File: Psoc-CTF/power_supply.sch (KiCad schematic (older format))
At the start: 17 parts, among them J1 Conn_01x02, J2 Conn_01x03, U1 AMS1117-5.0, U2 AMS1117-3.3, U6 AMS1117-3.3

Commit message: Corrrecciones y anexo de logo
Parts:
- added R46, R47: 0, Resistor_SMD:R_0805_2012Metric_Pad1.20x1.40mm_HandSolder, symbol Device:R
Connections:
- net +3V3: now also R47.2; no longer C40.1, U6.2 (VO)
- net +5V: now also R46.2; no longer U6.3 (VI)
- new net: C40.1, R47.1, U6.2 (VO)
- new net: R46.1, U6.3 (VI)
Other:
- moved on the sheet: C40, C41, U6
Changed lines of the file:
@@
 L power:+3V3 #PWR014
 U 1 1 62395ED8
-P 5075 4575
-F 0 "#PWR014" H 5075 4425 50  0001 C CNN
-F 1 "+3V3" H 5090 4748 50  0000 C CNN
-F 2 "" H 5075 4575 50  0001 C CNN
-F 3 "" H 5075 4575 50  0001 C CNN
-	1    5075 4575
+P 5250 4175
+F 0 "#PWR014" H 5250 4025 50  0001 C CNN
+F 1 "+3V3" H 5265 4348 50  0000 C CNN
+F 2 "" H 5250 4175 50  0001 C CNN
+F 3 "" H 5250 4175 50  0001 C CNN
+	1    5250 4175
 	1    0    0    -1
 $EndComp
-Connection ~ 4250 4875
+Connection ~ 4425 4475
 $Comp
 L power:GND #PWR013
 U 1 1 6239862F
-P 4250 4875
-F 0 "#PWR013" H 4250 4625 50  0001 C CNN
-F 1 "GND" H 4255 4702 50  0000 C CNN
-F 2 "" H 4250 4875 50  0001 C CNN
-F 3 "" H 4250 4875 50  0001 C CNN
-	1    4250 4875
+P 4425 4475
+F 0 "#PWR013" H 4425 4225 50  0001 C CNN
+F 1 "GND" H 4430 4302 50  0000 C CNN
+F 2 "" H 4425 4475 50  0001 C CNN
+F 3 "" H 4425 4475 50  0001 C CNN
+	1    4425 4475
 	1    0    0    -1
 $EndComp
-Connection ~ 4625 4875
+Connection ~ 4800 4475
 Wire Wire Line
-	4625 4875 5075 4875
+	4800 4475 5250 4475
 Wire Wire Line
-	4250 4875 4625 4875
-Connection ~ 4625 4575
+	4425 4475 4800 4475
 Wire Wire Line
-	4625 4575 5075 4575
-Wire Wire Line
-	4550 4575 4625 4575
+	4725 4175 4800 4175
 $Comp
 L Device:C C41
 U 1 1 6239863B
-P 5075 4725
-F 0 "C41" H 5190 4771 50  0000 L CNN
-F 1 "10uF" H 5190 4680 50  0000 L CNN
-F 2 "Capacitor_SMD:C_0603_1608Metric_Pad1.08x0.95mm_HandSolder" H 5113 4575 50  0001 C CNN
-F 3 "~" H 5075 4725 50  0001 C CNN
-	1    5075 4725
+P 5250 4325
+F 0 "C41" H 5365 4371 50  0000 L CNN
+F 1 "10uF" H 5365 4280 50  0000 L CNN
+F 2 "Capacitor_SMD:C_0603_1608Metric_Pad1.08x0.95mm_HandSolder" H 5288 4175 50  0001 C CNN
+F 3 "~" H 5250 4325 50  0001 C CNN
+	1    5250 4325
 	1    0    0    -1
 $EndComp
@@
 L Device:CP C40
 U 1 1 62398641
-P 4625 4725
-F 0 "C40" H 4743 4771 50  0000 L CNN
-F 1 "10uF" H 4743 4680 50  0000 L CNN
-F 2 "Capacitor_SMD:C_0805_2012Metric_Pad1.18x1.45mm_HandSolder" H 4663 4575 50  0001 C CNN
-F 3 "~" H 4625 4725 50  0001 C CNN
-	1    4625 4725
+P 4800 4325
+F 0 "C40" H 4918 4371 50  0000 L CNN
+F 1 "10uF" H 4918 4280 50  0000 L CNN
+F 2 "Capacitor_SMD:C_0805_2012Metric_Pad1.18x1.45mm_HandSolder" H 4838 4175 50  0001 C CNN
+F 3 "~" H 4800 4325 50  0001 C CNN
+	1    4800 4325
 	1    0    0    -1
 $EndComp
-Wire Wire Line
-	3800 4575 3950 4575
 $Comp
 L Regulator_Linear:AMS1117-3.3 U6
 U 1 1 62398648
-P 4250 4575
-F 0 "U6" H 4250 4817 50  0000 C CNN
-F 1 "AMS1117-3.3" H 4250 4726 50  0000 C CNN
-F 2 "Package_TO_SOT_SMD:SOT-223-3_TabPin2" H 4250 4775 50  0001 C CNN
-F 3 "http://www.advanced-monolithic.com/pdf/ds1117.pdf" H 4350 4325 50  0001 C CNN
-	1    4250 4575
+P 4425 4175
+F 0 "U6" H 4425 4417 50  0000 C CNN
+F 1 "AMS1117-3.3" H 4425 4326 50  0000 C CNN
+F 2 "Package_TO_SOT_SMD:SOT-223-3_TabPin2" H 4425 4375 50  0001 C CNN
+F 3 "http://www.advanced-monolithic.com/pdf/ds1117.pdf" H 4525 3925 50  0001 C CNN
+	1    4425 4175
 	1    0    0    -1
 $EndComp
-Text Notes 3900 4200 0    62   ~ 0
+Text Notes 4075 3800 0    62   ~ 0
 ESP POWER SUPPLY
 $Comp
 L power:+5V #PWR012
 U 1 1 62398656
-P 3800 4575
-F 0 "#PWR012" H 3800 4425 50  0001 C CNN
-F 1 "+5V" H 3800 4750 50  0000 C CNN
-F 2 "" H 3800 4575 50  0001 C CNN
-F 3 "" H 3800 4575 50  0001 C CNN
-	1    3800 4575
+P 3575 4150
+F 0 "#PWR012" H 3575 4000 50  0001 C CNN
+F 1 "+5V" H 3575 4325 50  0000 C CNN
+F 2 "" H 3575 4150 50  0001 C CNN
+F 3 "" H 3575 4150 50  0001 C CNN
+	1    3575 4150
 	1    0    0    -1
 $EndComp
-Connection ~ 5075 4575
+$Comp
+L Device:R R?
+U 1 1 624179B2
+P 3775 4175
+AR Path="/624179B2" Ref="R?"  Part="1"
+AR Path="/620E3406/624179B2" Ref="R46"  Part="1"
+F 0 "R46" V 3875 4175 50  0000 C CNN
+F 1 "0" V 3950 4175 50  0000 C CNN
+F 2 "Resistor_SMD:R_0805_2012Metric_Pad1.20x1.40mm_HandSolder" V 3705 4175 50  0001 C CNN
+F 3 "~" H 3775 4175 50  0001 C CNN
+	1    3775 4175
+	0    1    1    0
+$EndComp
+Wire Wire Line
+	3575 4150 3575 4175
+Wire Wire Line
+	3575 4175 3625 4175
+Wire Wire Line
+	3925 4175 4125 4175
+$Comp
+L Device:R R?
+U 1 1 62419A9D
+P 5025 4175
+AR Path="/62419A9D" Ref="R?"  Part="1"
+AR Path="/620E3406/62419A9D" Ref="R47"  Part="1"
+F 0 "R47" V 5125 4175 50  0000 C CNN
+F 1 "0" V 5200 4175 50  0000 C CNN
+F 2 "Resistor_SMD:R_0805_2012Metric_Pad1.20x1.40mm_HandSolder" V 4955 4175 50  0001 C CNN
+F 3 "~" H 5025 4175 50  0001 C CNN
+	1    5025 4175
+	0    -1   -1   0
+$EndComp
+Wire Wire Line
+	4875 4175 4800 4175
+Connection ~ 4800 4175
+Wire Wire Line
+	5175 4175 5250 4175
+Connection ~ 5250 4175
+Wire Notes Line
+	3450 3600 3450 4700
+Wire Notes Line
+	3450 4700 5600 4700
+Wire Notes Line
+	5600 4700 5600 3600
+Wire Notes Line
+	5600 3600 3450 3600
 $EndSCHEMATC

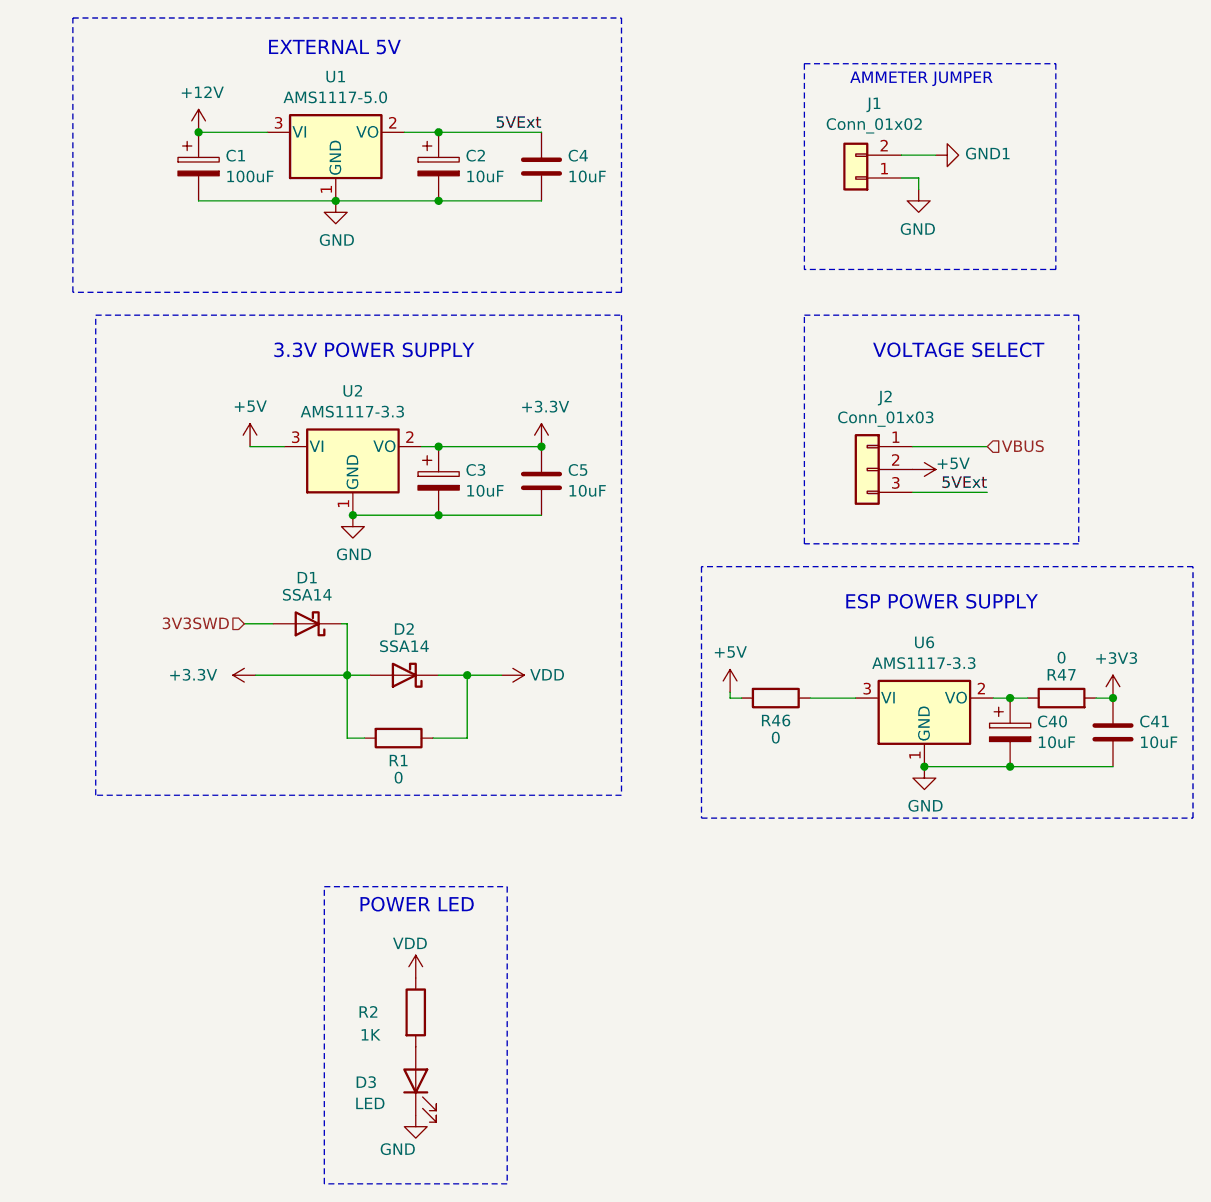
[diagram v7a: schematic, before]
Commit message: Correcciones del retorno de tiera y medicion de corriente
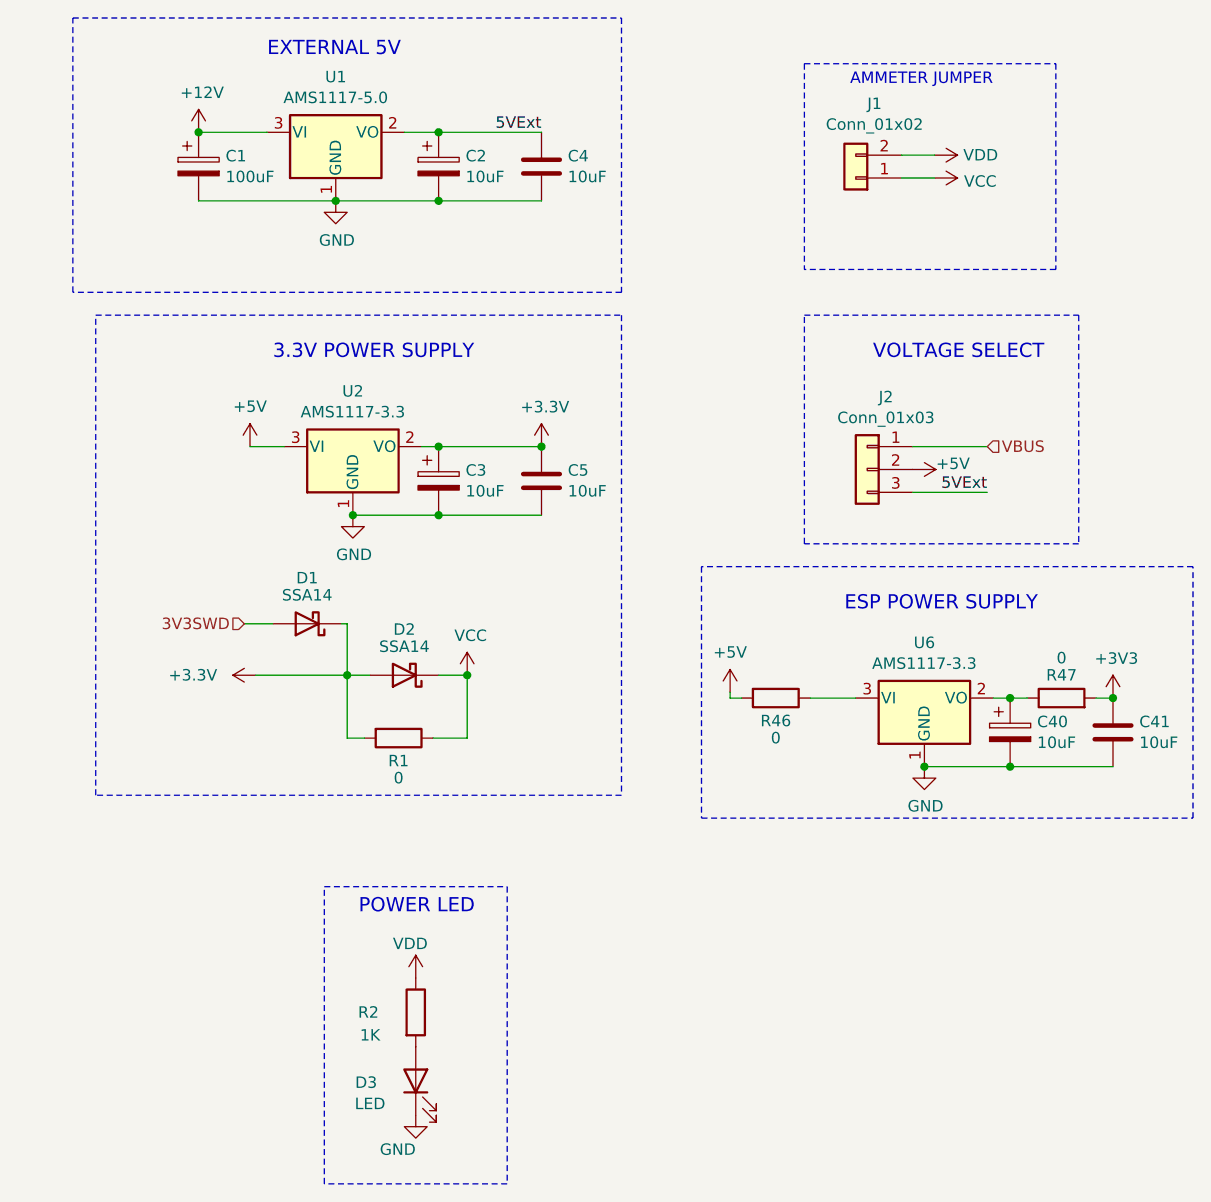
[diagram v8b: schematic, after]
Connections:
- net GND1 is gone; now on net VDD: J1.2 (Pin_2)
- net GND: no longer J1.1 (Pin_1)
- net VDD: no longer D2.1 (K), R1.1
- new net VCC: D2.1 (K), J1.1 (Pin_1), R1.1
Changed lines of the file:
@@
 L power:VDD #PWR?
 U 1 1 621106AB
-P 2575 4075
+P 4470 1800
 AR Path="/621106AB" Ref="#PWR?"  Part="1"
 AR Path="/620E3406/621106AB" Ref="#PWR08"  Part="1"
-F 0 "#PWR08" H 2575 3925 50  0001 C CNN
-F 1 "VDD" V 2575 4200 50  0000 L CNN
-F 2 "" H 2575 4075 50  0001 C CNN
-F 3 "" H 2575 4075 50  0001 C CNN
-	1    2575 4075
+F 0 "#PWR08" H 4470 1650 50  0001 C CNN
+F 1 "VDD" V 4470 1925 50  0000 L CNN
+F 2 "" H 4470 1800 50  0001 C CNN
+F 3 "" H 4470 1800 50  0001 C CNN
+	1    4470 1800
 	0    1    1    0
 $EndComp
@@
 Text Notes 1950 5125 0    62   ~ 0
 POWER LED
-Wire Wire Line
-	4325 1800 4475 1800
-$Comp
-L power:GND #PWR?
-U 1 1 621350E1
-P 4400 1950
-AR Path="/621350E1" Ref="#PWR?"  Part="1"
-AR Path="/620E3406/621350E1" Ref="#PWR011"  Part="1"
-F 0 "#PWR011" H 4400 1700 50  0001 C CNN
-F 1 "GND" H 4475 1775 50  0000 R CNN
-F 2 "" H 4400 1950 50  0001 C CNN
-F 3 "" H 4400 1950 50  0001 C CNN
-	1    4400 1950
-	1    0    0    -1
-$EndComp
 $Comp
 L Connector_Generic:Conn_01x02 J?
@@
 Wire Wire Line
 	2425 4350 2425 4075
-Connection ~ 2425 4075
-Wire Wire Line
-	2425 4075 2575 4075
 $Comp
 L Device:D_Schottky D1
@@
 Wire Notes Line
 	3100 2400 700  2400
-Wire Wire Line
-	4325 1900 4400 1900
-Wire Wire Line
-	4400 1900 4400 1950
-$Comp
-L power:GND1 #PWR056
-U 1 1 622A7FA3
-P 4475 1800
-F 0 "#PWR056" H 4475 1550 50  0001 C CNN
-F 1 "GND1" V 4480 1672 50  0000 R CNN
-F 2 "" H 4475 1800 50  0001 C CNN
-F 3 "" H 4475 1800 50  0001 C CNN
-	1    4475 1800
-	0    -1   -1   0
-$EndComp
 $Comp
 L power:+3V3 #PWR014
@@
 Wire Notes Line
 	5600 3600 3450 3600
+$Comp
+L power:VCC #PWR?
+U 1 1 625A031E
+P 2425 4075
+F 0 "#PWR?" H 2425 3925 50  0001 C CNN
+F 1 "VCC" H 2440 4248 50  0000 C CNN
+F 2 "" H 2425 4075 50  0001 C CNN
+F 3 "" H 2425 4075 50  0001 C CNN
+	1    2425 4075
+	1    0    0    -1
+$EndComp
+Connection ~ 2425 4075
+$Comp
+L power:VCC #PWR?
+U 1 1 625A2413
+P 4470 1900
+F 0 "#PWR?" H 4470 1750 50  0001 C CNN
+F 1 "VCC" V 4485 2028 50  0000 L CNN
+F 2 "" H 4470 1900 50  0001 C CNN
+F 3 "" H 4470 1900 50  0001 C CNN
+	1    4470 1900
+	0    1    1    0
+$EndComp
+Wire Wire Line
+	4325 1900 4470 1900
+Wire Wire Line
+	4325 1800 4470 1800
 $EndSCHEMATC
